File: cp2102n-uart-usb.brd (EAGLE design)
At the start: 36 x 18 mm, 29 parts, among them IC1 CP2102N-A02-GQFN24, J1 USB4105-GF-A, J2 61300611021

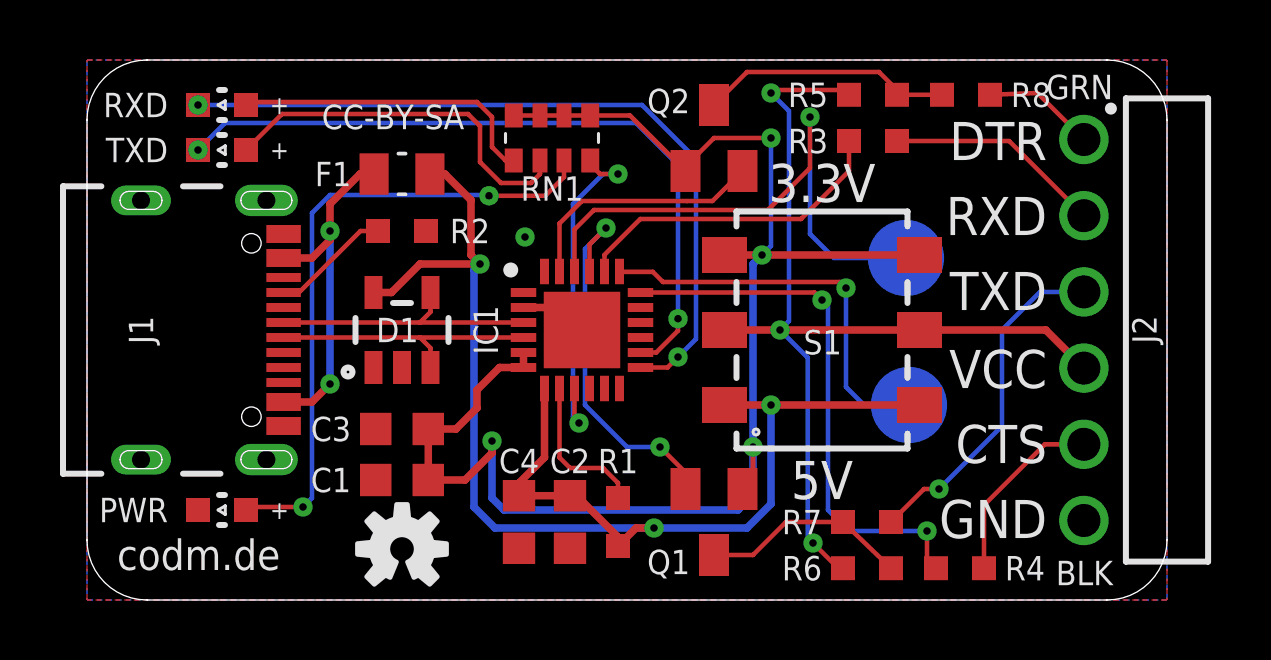
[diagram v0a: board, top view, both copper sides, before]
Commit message: added 5k1 to CC2
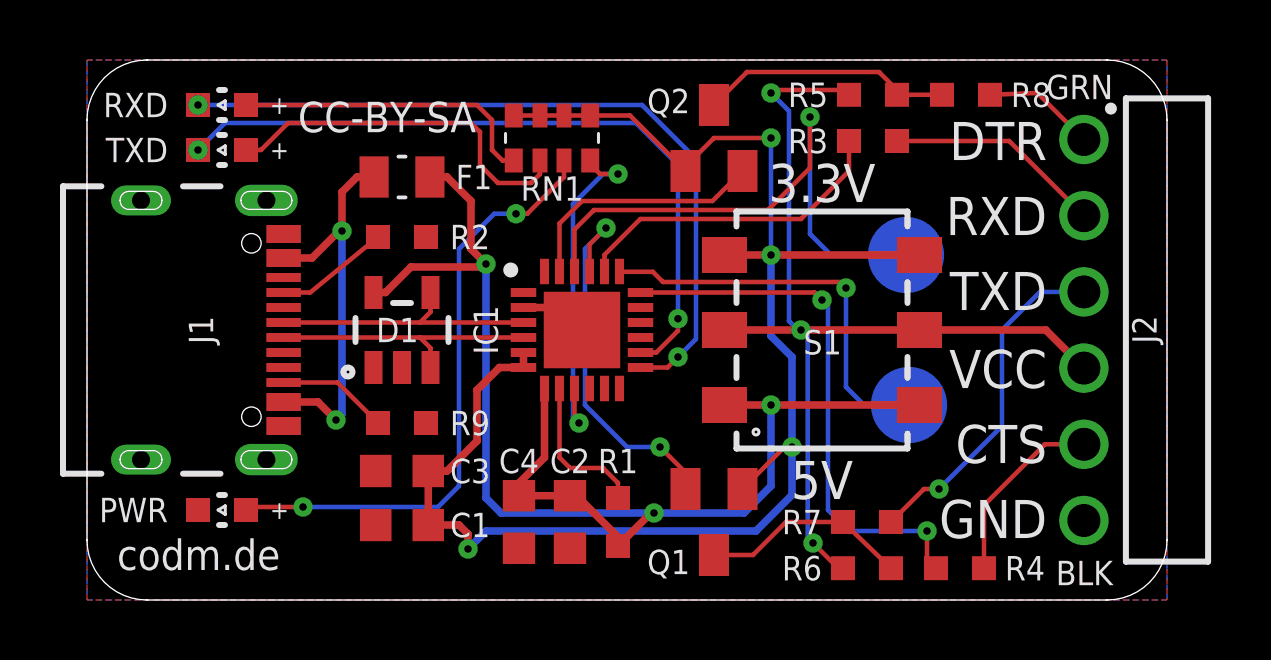
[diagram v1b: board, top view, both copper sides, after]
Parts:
- removed U$3: (no value), SparkFun-Aesthetics:OSHW-LOGO-S
- added R9: 5k1, codm:R0603RF
- moved C1 1.50 mm to (10.5, 2.50)
- moved C3 1.40 mm to (10.5, 4.30)
- moved R2 0.20 mm to (10.5, 12.1)
- moved DSR 0.10 mm to (27.3, 11.5)
- moved F1 0.10 mm to (10.5, 14.1)
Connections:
- new net N$5: J1.B5, R9.2
- net GND: now also R9.1
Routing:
- net N$5: track 0.00 -> 3.70 mm
- net +3V3: track 50.5 -> 52.2 mm
- net N$7: track 11.8 -> 13.3 mm
- net +5V: track 46.0 -> 45.0 mm
- net N$15: track 21.3 -> 20.4 mm
- net GND: vias 1 -> 0
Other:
- board text added: "90100-0.2"
- board text removed: "90100-0.1"
